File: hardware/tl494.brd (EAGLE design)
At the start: 100 x 80 mm, 91 parts, among them IC1 TL494CN, J1 CON_HEADER_1X02-PTH, J2 CON_HEADER_1X02-PTH, J3 J20MM, J4 J5MM, J5 J15MM, K2 24V, Q1 2N5551, Q1I 8050, Q1I1 2N3904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

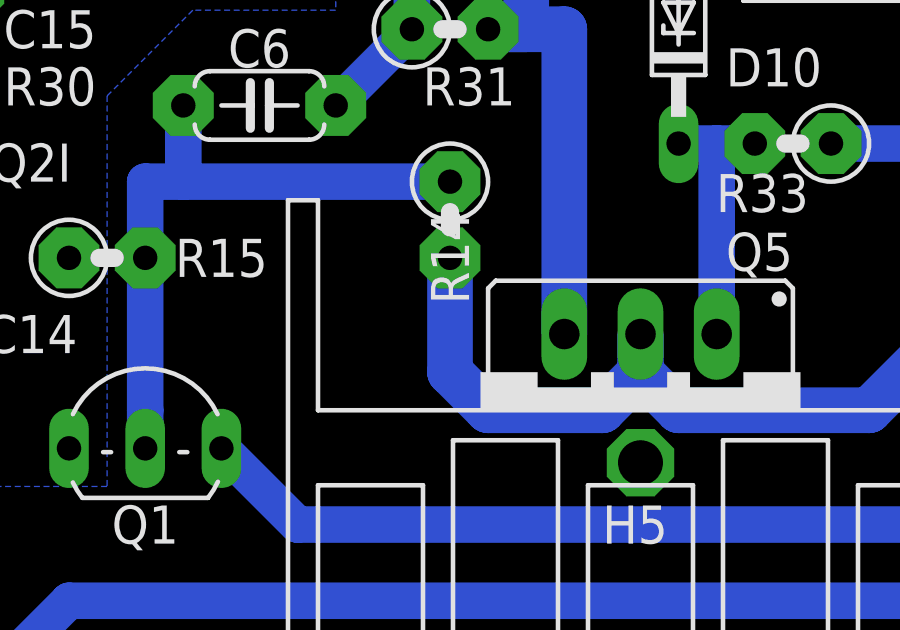
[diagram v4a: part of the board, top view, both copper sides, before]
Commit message: new bootstrap circuit doc
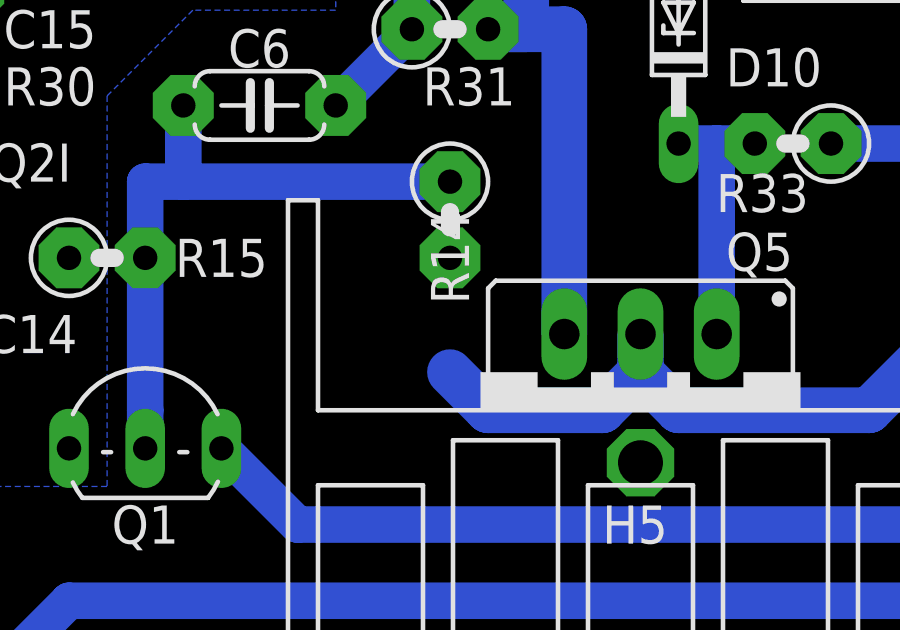
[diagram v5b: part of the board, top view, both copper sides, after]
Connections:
- net +15V: now also D5.A, R14.2
- net +V: no longer D5.A, R14.2
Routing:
- net +V: track 53.8 -> 50.0 mm
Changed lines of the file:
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@@
 <?xml version="1.0" encoding="utf-8"?>
 <!DOCTYPE eagle SYSTEM "eagle.dtd">
-<eagle version="9.4.2">
+<eagle version="9.1.3">
 <drawing>
 <settings>
@@
 <contactref element="C11" pad="+"/>
 <contactref element="Q4" pad="2"/>
-<contactref element="D5" pad="A"/>
-<contactref element="R14" pad="2"/>
 <contactref element="K2" pad="P"/>
 <contactref element="R33" pad="1"/>
@@
 <wire x1="30.48" y1="17.78" x2="29.21" y2="19.05" width="1.524" layer="16"/>
 <wire x1="34.29" y1="17.78" x2="30.48" y2="17.78" width="1.524" layer="16"/>
-<wire x1="29.21" y1="19.05" x2="29.21" y2="22.86" width="1.524" layer="16"/>
 <wire x1="41.91" y1="26.67" x2="45.085" y2="26.67" width="1.2192" layer="16"/>
 <wire x1="48.30220625" y1="43.18" x2="45.085" y2="39.96279375" width="1.524" layer="16"/>
 <wire x1="45.085" y1="39.96279375" x2="45.085" y2="26.67" width="1.524" layer="16"/>
 <wire x1="49.53" y1="43.18" x2="48.30220625" y2="43.18" width="1.524" layer="16"/>
+<wire x1="80.01" y1="41.275" x2="85.455" y2="49.53" width="0" layer="19" extent="1-1"/>
+<wire x1="65.405" y1="49.53" x2="80.01" y2="41.275" width="0" layer="19" extent="1-1"/>
+<wire x1="53.975" y1="51.435" x2="65.405" y2="49.53" width="0" layer="19" extent="1-1"/>
+<wire x1="49.53" y1="43.18" x2="53.975" y2="51.435" width="0" layer="19" extent="1-1"/>
 </signal>
 <signal name="N$10">
@@
 <wire x1="31.75" y1="30.48" x2="30.48" y2="30.48" width="1.524" layer="16"/>
 <wire x1="31.75" y1="35.56" x2="31.75" y2="30.48" width="1.524" layer="16"/>
+<contactref element="D5" pad="A"/>
+<contactref element="R14" pad="2"/>
+<wire x1="31.75" y1="35.56" x2="58.42" y2="41.91" width="0" layer="19" extent="1-1"/>
+<wire x1="29.21" y1="22.86" x2="33.02" y2="20.32" width="0" layer="19" extent="1-1"/>
 </signal>
 <signal name="VIN">

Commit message: 1
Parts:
- R14: value 130K -> 68K
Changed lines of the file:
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@@
 <?xml version="1.0" encoding="utf-8"?>
 <!DOCTYPE eagle SYSTEM "eagle.dtd">
-<eagle version="9.1.3">
+<eagle version="9.4.2">
 <drawing>
 <settings>
@@
 <attribute name="VALUE" x="13.335" y="33.2994" size="1.27" layer="27" ratio="10" rot="R90"/>
 </element>
-<element name="R14" library="trosh_devices.eagle.v9" package="0207/2V_EXPAD" value="130K" x="29.21" y="24.13" smashed="yes" rot="R270">
+<element name="R14" library="trosh_devices.eagle.v9" package="0207/2V_EXPAD" value="68K" x="29.21" y="24.13" smashed="yes" rot="R270">
 <attribute name="NAME" x="29.21" y="22.86" size="1.27" layer="25" ratio="10" rot="R270" align="center"/>
 <attribute name="VALUE" x="28.575" y="26.3906" size="1.27" layer="27" ratio="10" rot="R270"/>

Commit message: 2
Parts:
- R18: value 2K 1W -> 470R 1W
- R19: value 4K 1/2W -> 1K 1/2W
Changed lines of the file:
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@@
 <attribute name="VALUE" x="52.4256" y="35.56" size="1.27" layer="27" ratio="10" rot="R180"/>
 </element>
-<element name="R18" library="trosh_devices.eagle.v9" package="0414V_EXPAD" value="2K 1W" x="66.675" y="38.1" smashed="yes">
+<element name="R18" library="trosh_devices.eagle.v9" package="0414V_EXPAD" value="470R 1W" x="66.675" y="38.1" smashed="yes">
 <attribute name="NAME" x="67.31" y="40.005" size="1.27" layer="25" ratio="10" align="center"/>
 <attribute name="VALUE" x="64.4144" y="37.465" size="1.27" layer="27" ratio="10"/>
 </element>
-<element name="R19" library="trosh_devices.eagle.v9" package="0414V_EXPAD" value="4K 1/2W" x="66.675" y="33.02" smashed="yes" rot="R90">
+<element name="R19" library="trosh_devices.eagle.v9" package="0414V_EXPAD" value="1K 1/2W" x="66.675" y="33.02" smashed="yes" rot="R90">
 <attribute name="NAME" x="69.85" y="30.48" size="1.27" layer="25" ratio="10" rot="R90" align="center"/>
 <attribute name="VALUE" x="67.31" y="30.7594" size="1.27" layer="27" ratio="10" rot="R90"/>

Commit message: 1
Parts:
- added C18: 100uF 25V, trosh_devices.eagle.v9:E2,5-7_EXPAD
- added D6: 13V 1/4W, diode:DO34Z7
- added J6, J7, J8: J5MM, jumper:05
- added Q7: 2N3904, dp_devices.v6:TO-92
- added R23: 10K, trosh_devices.eagle.v9:0207/2V_EXPAD
- added R24: 470R 1W, trosh_devices.eagle.v9:0414V_EXPAD
- C16: value 100uF 25V -> 10uF 50V
- D10: value 16V 1/4W -> 21V 1/4W
- D2: value FR107 -> RGP15J; device trosh_devices.eagle.v9:RAD2,5_EXPAD -> diode:DO41-10
- D3: value FCH30A06 -> FCHS20A08
- D4: value 1N4148 -> FR107; device trosh_devices.eagle.v9:DO35-20 -> diode:DO41-10
- R19: value 1K 1/2W -> 1K 5W
- R33: value 100K -> 10K
- moved D4 44.1 mm to (33.0, 44.5), turned to 0 degrees
- moved D5 21.8 mm to (45.7, 29.2)
- moved RT1 21.6 mm to (38.1, 63.5), turned to 0 degrees
- moved D2 12.7 mm to (53.3, 21.6), turned to 270 degrees
- moved R3 11.7 mm to (29.2, 72.4)
- moved D9 11.4 mm to (29.2, 74.9)
- moved R14 9.25 mm to (20.3, 21.6)
- moved R21 8.91 mm to (13.3, 71.1)
- moved C16 8.26 mm to (33.0, 27.3), turned to 90 degrees
- moved R11 7.62 mm to (12.7, 63.5)
- moved C7 5.39 mm to (61.0, 40.6)
- moved R5 5.24 mm to (6.35, 67.3)
- moved D1 5.08 mm to (21.6, 66.0)
- moved R2 5.08 mm to (8.89, 55.9)
- moved C1 5.08 mm to (7.62, 72.4)
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- renumbered Q1I to Q8, Q1I1 to Q10, Q2I to Q9
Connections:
- removed net +15V: C16.+, C4.2, D5.A, IC1.12, Q5.3, R14.2, R31.2
- removed net +V: C10.+, C11.+, C9.1, K2.P, Q4.2, Q5.2, R33.1
- new net +12.4V: C4.2, D4.C, IC1.12, R24.1, R31.2
- new net +21.6V: C16.+, D5.A, Q5.3, R14.2
- new net +48V: C10.+, C11.+, C9.1, J7.1, K2.P, Q4.2, Q5.2, R33.1
- new net N$40: D6.C, Q7.2, R23.2
- new net N$41: C18.+, Q7.1, R24.2
- new net N$42: D5.C, J6.1
- new net N$43: J7.2, Q7.3, R23.1
- new net N$44: D4.A, J8.2
- net GND: now also C18.-, D6.A
- net N$18: no longer D4.C
- net N$19: now also J6.2; no longer D5.C
- net VOUT: now also J8.1; no longer D4.A
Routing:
- net +V: track 50.0 -> 0.00 mm
- net +48V: track 0.00 -> 45.9 mm
- net +15V: track 30.3 -> 0.00 mm
- net +21.6V: track 0.00 -> 27.4 mm
- net VOUT: track 156.0 -> 177.4 mm
- net +12.4V: track 0.00 -> 18.8 mm
- net N$41: track 0.00 -> 14.9 mm
- net N$28: track 51.9 -> 65.5 mm
- net N$13: track 21.6 -> 11.4 mm
- net N$18: track 26.8 -> 16.7 mm
- net N$40: track 0.00 -> 9.83 mm
- net N$43: track 0.00 -> 9.20 mm
- net N$44: track 0.00 -> 8.41 mm
- net N$17: track 17.1 -> 24.7 mm
- net N$10: track 13.5 -> 20.7 mm
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- added copper zone on layer 16, net +48V
- removed copper zone on layer 16, net +V
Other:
- board text added: "02-01-2020"
- board text added: "LEADTECH CSPG 48V DC-DC MODULE V1.0c"
- board text removed: "01-11-2020"
- board text removed: "LEADTECH CSPG 48V DC-DC MODULE V1.0b"
